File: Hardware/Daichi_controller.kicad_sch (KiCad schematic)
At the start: 24 parts, among them J1 USB_B_Mini, J2 S21, Q1 BF545A

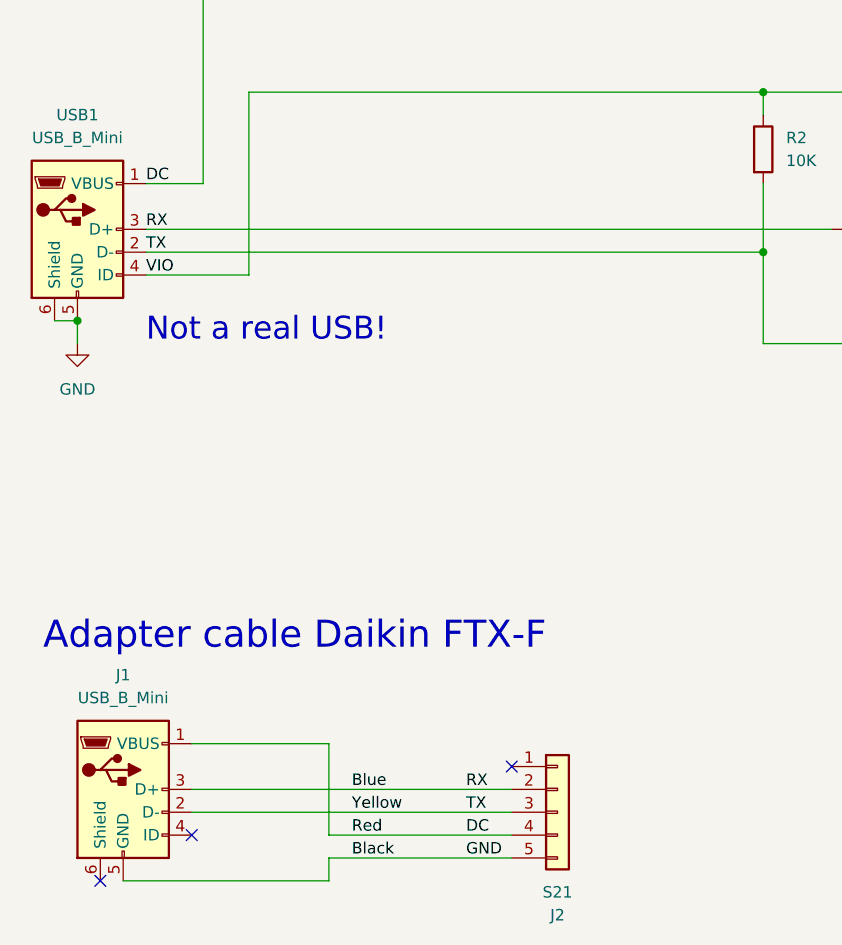
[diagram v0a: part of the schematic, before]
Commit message: Hardware: Update schematic
Notes on voltages, measured on my aircon. Can be important.
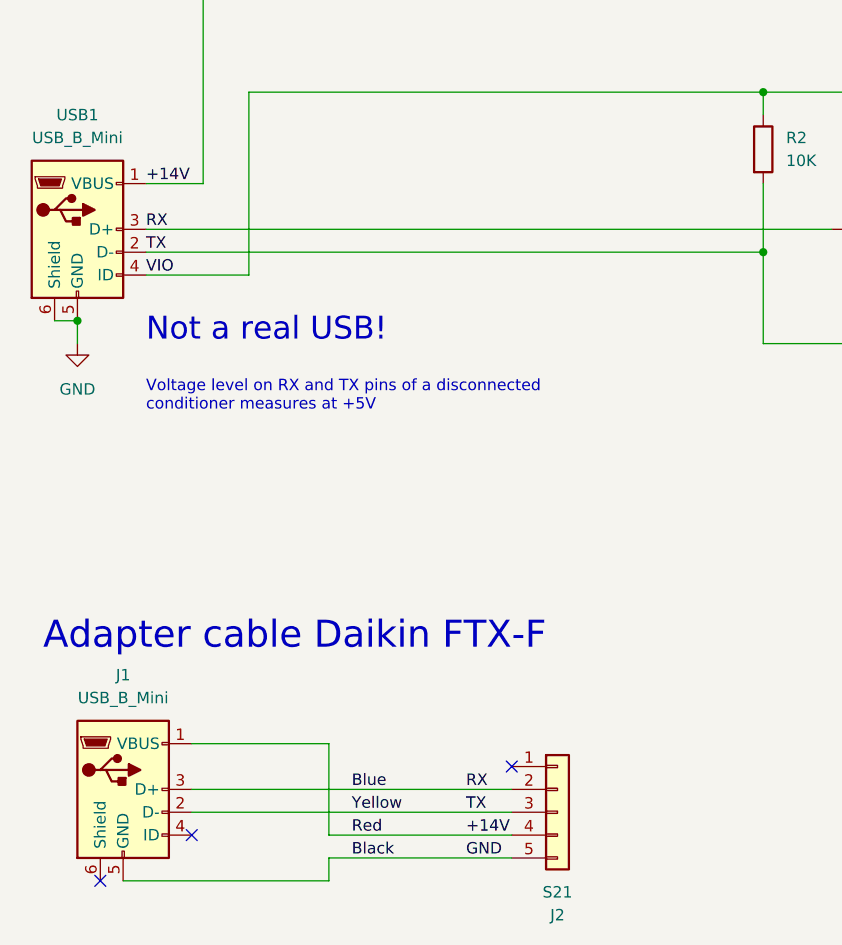
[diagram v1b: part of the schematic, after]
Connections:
- net DC renamed +14V
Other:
- note added: "Voltage level on RX and TX pins of a disconnected conditioner measures at +5V"
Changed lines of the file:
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@@
     (stroke (width 0) (type default))
+  )
+  (text "Voltage level on RX and TX pins of a disconnected\nconditioner measures at +5V"
+    (at 33.02 127 0)
+    (effects (font (size 1.27 1.27)) (justify left bottom))
   )
   (text "Adapter cable Daikin FTX-F" (at 21.59 153.67 0)
@@
     (effects (font (size 1.27 1.27)) (justify left bottom))
   )
-  (label "DC" (at 33.02 101.6 0) (fields_autoplaced)
+  (label "+14V" (at 33.02 101.6 0) (fields_autoplaced)
     (effects (font (size 1.27 1.27)) (justify left bottom))
   )
-  (label "DC" (at 68.58 173.99 0) (fields_autoplaced)
+  (label "+14V" (at 68.58 173.99 0) (fields_autoplaced)
     (effects (font (size 1.27 1.27)) (justify left bottom))
   )
